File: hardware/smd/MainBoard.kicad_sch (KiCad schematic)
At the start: 52 parts, among them J10 B2_HDR, J11 B2_HDR, J12 ISP, J9 POWER_HDR, Q1 MMBT3904, Q2 MMBT3904, Q3 MMBT3904, U1 ATtiny85, U2 TL074, U3 78L05, U4 79L05

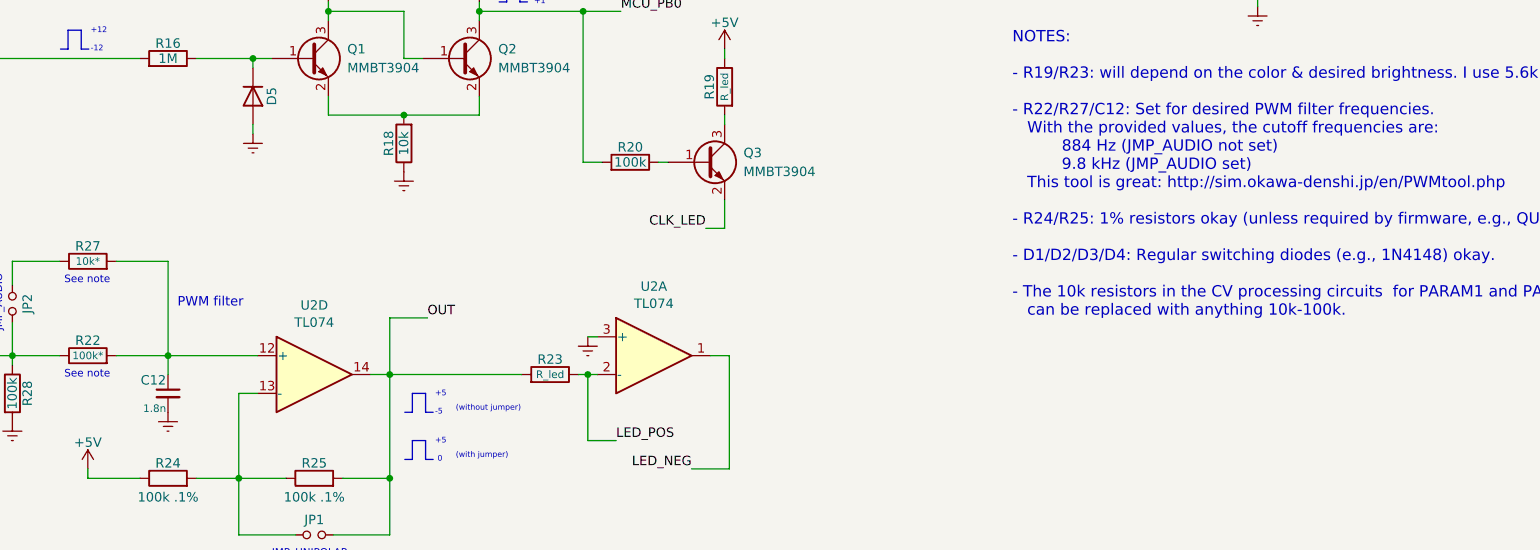
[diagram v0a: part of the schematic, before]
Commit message: Change C12 to 2.2nF, matching LCSC part code.
Flag some non-SMD parts as exclude from position file.
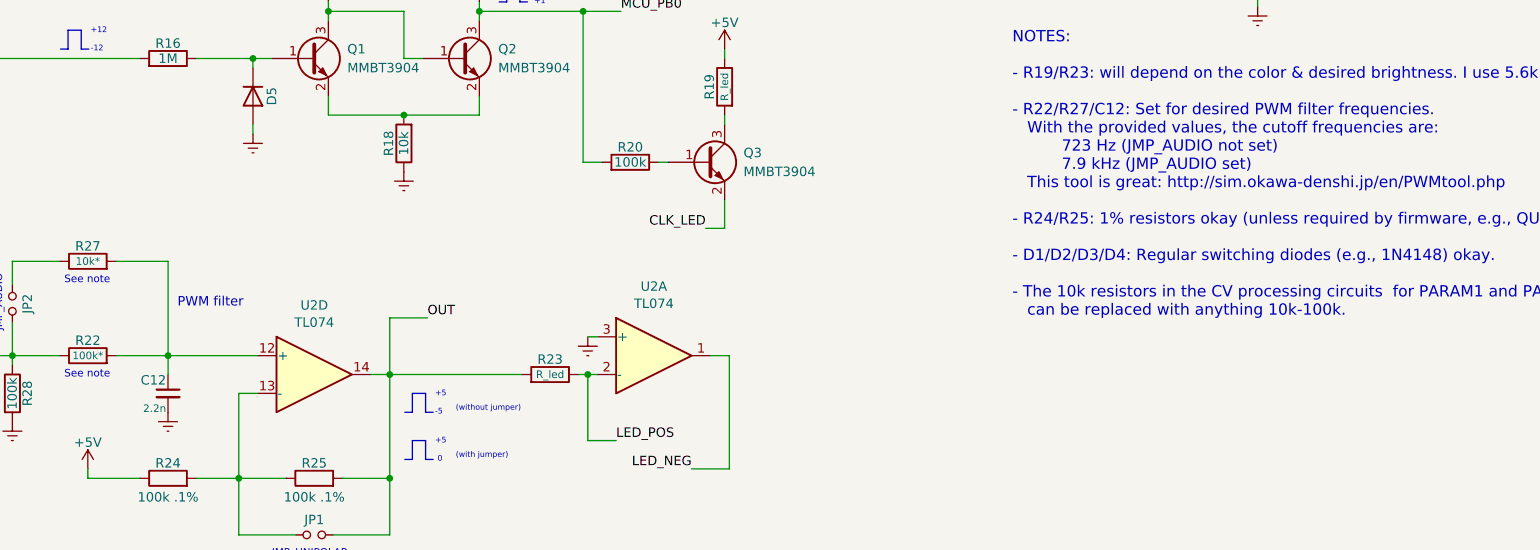
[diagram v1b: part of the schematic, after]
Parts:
- C12: value 1.8n -> 2.2n
- D10, D11: SMT package SOD-123 -> SOD-323
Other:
- note added: "NOTES: - R19/R23: will depend on the color & desired brightness. I use 5.6k for my red LEDs. - R22/R27/C12: Set for desired PWM filter frequencies. With the provided values, the cutoff frequencies are: 723 Hz (JMP_AUDIO not set) 7.9 kHz (JMP_AUDIO set) This tool is great: http://sim.okawa-denshi.jp/en/PWMtool.php - R24/R25: 1% resistors okay (unless required by firmware, e.g., QUANT) - D1/D2/D3/D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"
- note removed: "NOTES: - R19/R23: will depend on the color & desired brightness. I use 5.6k for my red LEDs. - R22/R27/C12: Set for desired PWM filter frequencies. With the provided values, the cutoff frequencies are: 884 Hz (JMP_AUDIO not set) 9.8 kHz (JMP_AUDIO set) This tool is great: http://sim.okawa-denshi.jp/en/PWMtool.php - R24/R25: 1% resistors okay (unless required by firmware, e.g., QUANT) - D1/D2/D3/D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"
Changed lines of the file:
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@@
     (effects (font (size 1.778 1.778) (thickness 0.3556) bold) (justify left bottom))
   )
-  (text "NOTES:\n\n- R19/R23: will depend on the color & desired brightness. I use 5.6k for my red LEDs.\n\n- R22/R27/C12: Set for desired PWM filter frequencies.\n   With the provided values, the cutoff frequencies are:\n          884 Hz (JMP_AUDIO not set)\n          9.8 kHz (JMP_AUDIO set)\n   This tool is great: http://sim.okawa-denshi.jp/en/PWMtool.php\n\n- R24/R25: 1% resistors okay (unless required by firmware, e.g., QUANT)\n\n- D1/D2/D3/D4: Regular switching diodes (e.g., 1N4148) okay.\n\n- The 10k resistors in the CV processing circuits  for PARAM1 and PARAM2\n   can be replaced with anything 10k-100k."
+  (text "NOTES:\n\n- R19/R23: will depend on the color & desired brightness. I use 5.6k for my red LEDs.\n\n- R22/R27/C12: Set for desired PWM filter frequencies.\n   With the provided values, the cutoff frequencies are:\n          723 Hz (JMP_AUDIO not set)\n          7.9 kHz (JMP_AUDIO set)\n   This tool is great: http://sim.okawa-denshi.jp/en/PWMtool.php\n\n- R24/R25: 1% resistors okay (unless required by firmware, e.g., QUANT)\n\n- D1/D2/D3/D4: Regular switching diodes (e.g., 1N4148) okay.\n\n- The 10k resistors in the CV processing circuits  for PARAM1 and PARAM2\n   can be replaced with anything 10k-100k."
     (at 177.165 162.56 0)
     (effects (font (size 1.524 1.524)) (justify left bottom))
@@
       (effects (font (size 1.27 1.27)) (justify left))
     )
-    (property "Value" "1.8n" (at 63.246 174.752 0)
+    (property "Value" "2.2n" (at 63.246 174.752 0)
       (effects (font (size 1.016 1.016)) (justify left))
     )
@@
       (effects (font (size 1.27 1.27)) hide)
     )
-    (property "Datasheet" "~" (at 175.26 26.67 0)
+    (property "Datasheet" "" (at 175.26 26.67 0)
       (effects (font (size 1.27 1.27)) hide)
     )
@@
       (effects (font (size 1.27 1.27)) hide)
     )
-    (property "SMT package" "SOD-123" (at 175.26 26.67 0)
+    (property "SMT package" "SOD-323" (at 175.26 26.67 0)
       (effects (font (size 1.27 1.27)) hide)
     )
@@
       (effects (font (size 1.27 1.27)) hide)
     )
-    (property "Datasheet" "~" (at 175.26 44.45 0)
+    (property "Datasheet" "" (at 175.26 44.45 0)
       (effects (font (size 1.27 1.27)) hide)
     )
@@
       (effects (font (size 1.27 1.27)) hide)
     )
-    (property "SMT package" "SOD-123" (at 175.26 44.45 0)
+    (property "SMT package" "SOD-323" (at 175.26 44.45 0)
       (effects (font (size 1.27 1.27)) hide)
     )

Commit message: Fix footprint for ATtiny85 (wide SOIC-8).
Add "JLCPCB Rotation Offset" field with rotations for U and Q components.
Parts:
- Q1, Q2, Q3, U3, U4: JLCPCB Rotation Offset (none) -> 180
- U1: footprint Package_SO:SOIC-8_3.9x4.9mm_P1.27mm -> Package_SO:SOIC-8W_5.3x5.3mm_P1.27mm; JLCPCB Rotation Offset (none) -> 90
- U2: JLCPCB Rotation Offset (none) -> 90
